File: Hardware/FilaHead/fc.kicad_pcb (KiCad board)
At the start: 2 copper layers, 55.9 x 48.3 mm, 7 parts, among them J0 Conn_2, J1 Conn_01x15_Female, J2 Conn_01x15_Female, J3 Conn_2

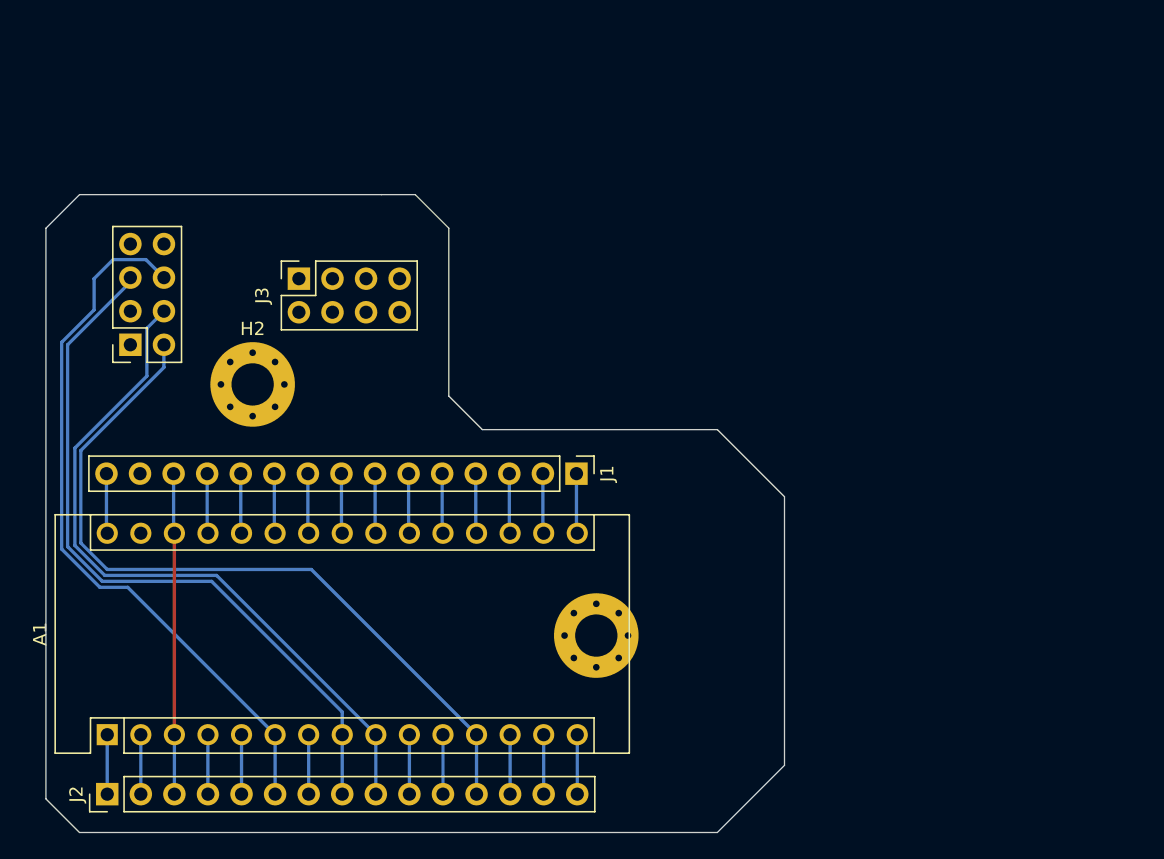
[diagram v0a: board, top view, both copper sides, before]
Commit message: Updated Fila Head
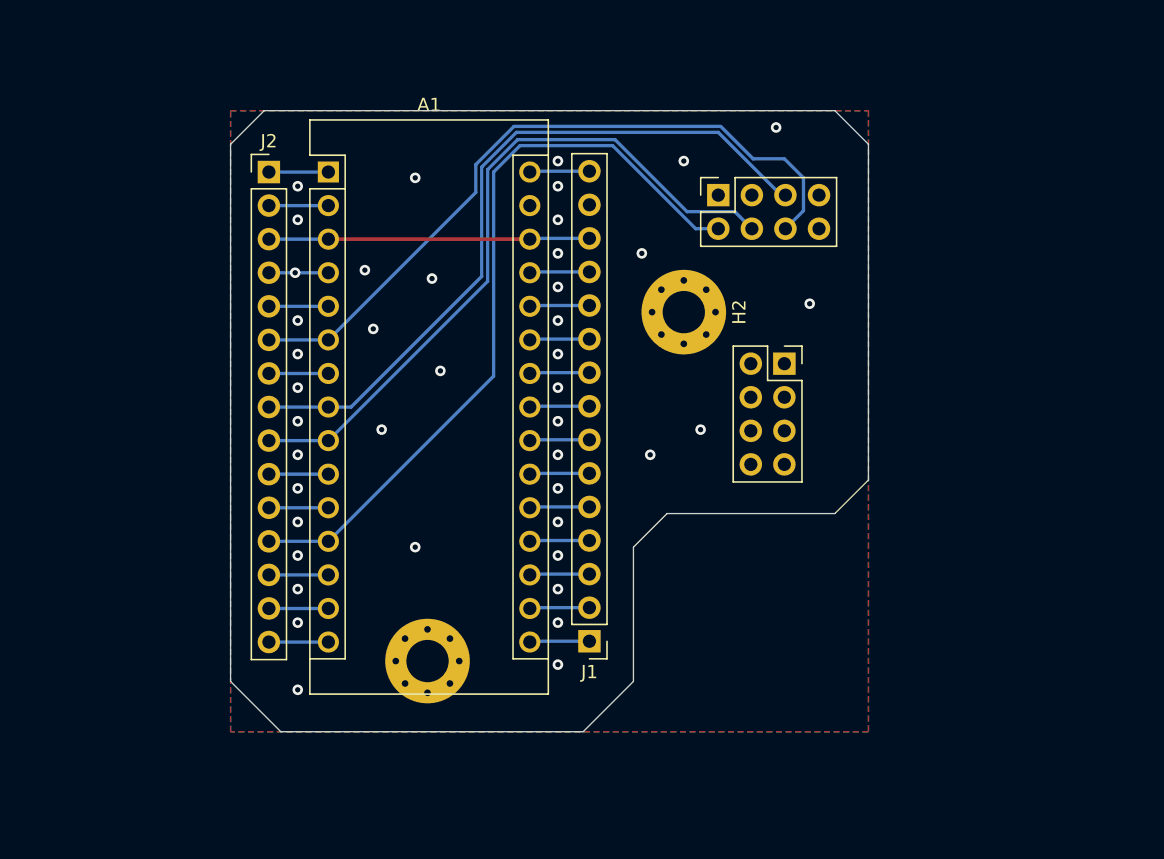
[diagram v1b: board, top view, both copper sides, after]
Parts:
- moved J2 48.6 mm to (103.2, 38.9), turned to 0 degrees
- moved J0 45.9 mm to (137.2, 40.7), turned to 90 degrees
- moved A1 45.7 mm to (107.7, 38.9), turned to 0 degrees
- moved J3 37.3 mm to (142.2, 53.4), turned to 0 degrees
- moved H2 33.1 mm to (134.6, 49.5), turned to 270 degrees
- moved H1 12.9 mm to (115.2, 75.9), turned to 270 degrees
- moved J1 12.7 mm to (127.5, 74.4), turned to 180 degrees
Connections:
- J0 pad 3: Net-(J0-Pad3) -> (no net)
- J0 pad 7: Net-(J0-Pad7) -> (no net)
- J3 pad 2: Net-(J3-Pad2) -> (no net)
- J3 pad 3: Net-(J3-Pad3) -> (no net)
- J3 pad 4: Net-(J3-Pad4) -> (no net)
- J3 pad 5: Net-(J3-Pad5) -> (no net)
- J3 pad 6: Net-(J3-Pad6) -> (no net)
- J3 pad 7: Net-(J3-Pad7) -> (no net)
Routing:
- net GND: vias 0 -> 43
- added copper zone on B.Cu, net GND
- added copper zone on F.Cu, net GND
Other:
- board size 55.9 x 48.3 mm -> 48.3 x 47 mm

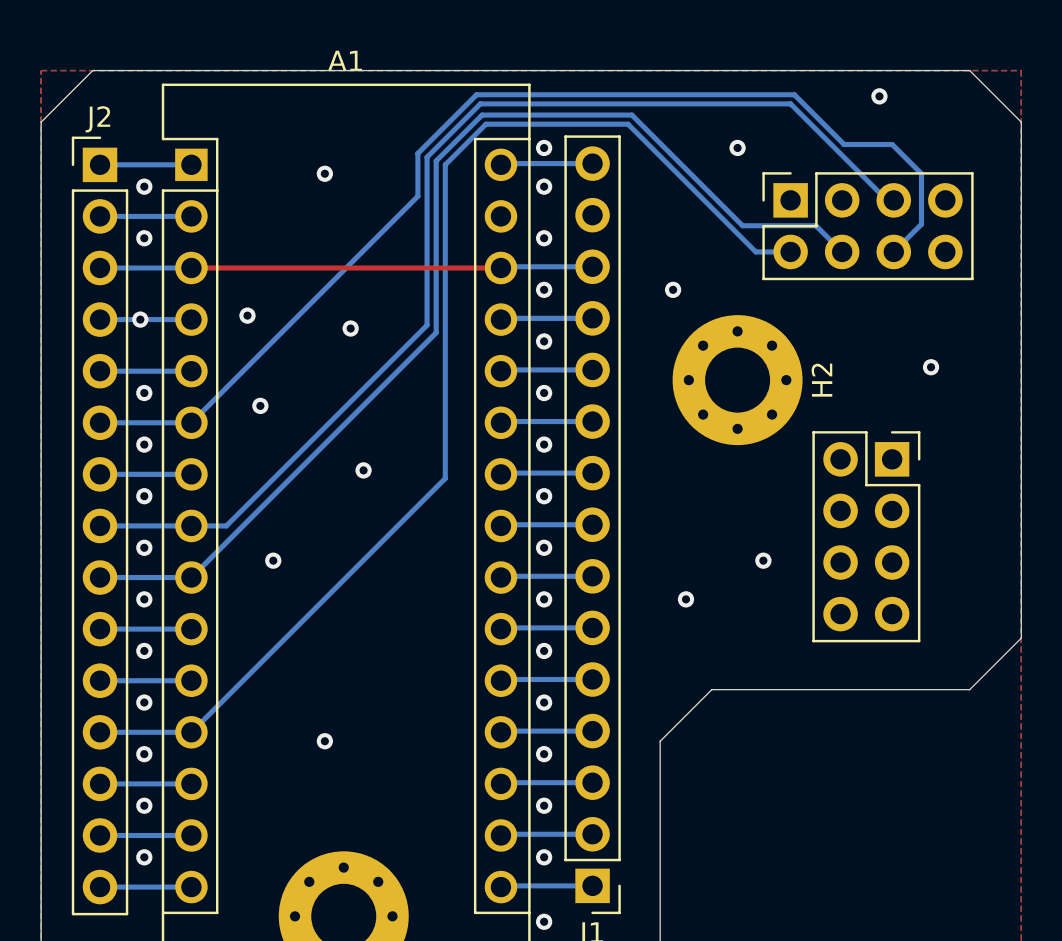
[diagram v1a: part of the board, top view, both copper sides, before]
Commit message: updated and generated Header connector
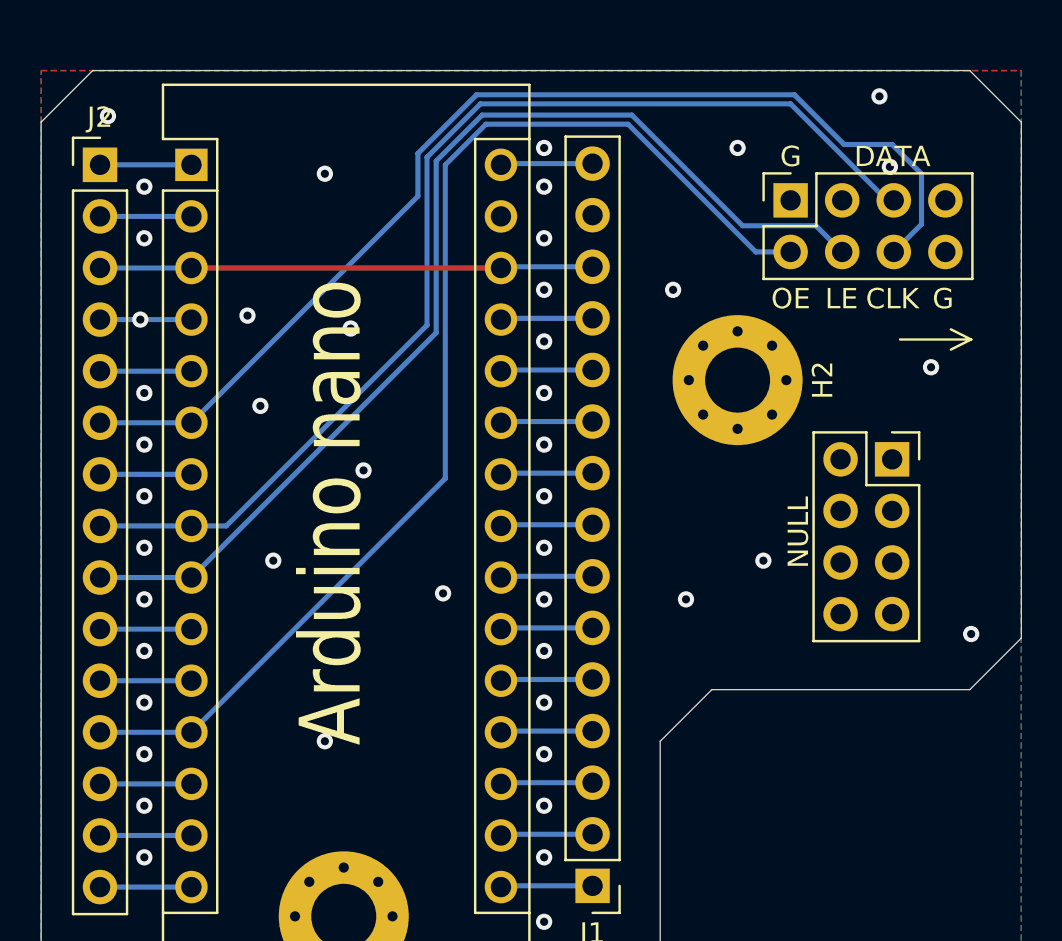
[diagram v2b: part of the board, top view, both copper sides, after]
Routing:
- net GND: vias 43 -> 47
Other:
- rule pad_to_mask_clearance: 0.051 -> 0
- board text added: "Arduino nano"
- board text added: "CLK"
- board text added: "DATA"
- board text added: "Filament Wall (2021.04) Header Connector v0.1 Sandbox Workshop Designed by Caorx Wangyw"
- board text added: "G"
- board text added: "JLCJLCJLCJLC"
- board text added: "LE"
- board text added: "NULL"
- board text added: "OE"

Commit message: updated packages
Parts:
- J0, J3: footprint Connector_PinSocket_2.54mm:PinSocket_2x04_P2.54mm_Vertical -> Connector_PinHeader_2.54mm:PinHeader_2x04_P2.54mm_Vertical
- moved J3 2.53 mm to (139.7, 53.3)
- moved J0 2.50 mm to (137.2, 43.2)
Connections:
- J0 pad 1: GND -> OE
- J0 pad 2: OE -> GND
- J0 pad 3: (no net) -> LE
- J0 pad 4: LE -> Net-(J0-Pad4)
- J0 pad 5: PWM5 -> CLK
- J0 pad 6: CLK -> PWM5
- J0 pad 7: (no net) -> GND
- J0 pad 8: GND -> Net-(J0-Pad8)
- J3 pad 1: GND -> Net-(J3-Pad1)
- J3 pad 2: (no net) -> GND
- J3 pad 3: (no net) -> Net-(J3-Pad3)
- J3 pad 4: (no net) -> Net-(J3-Pad4)
- J3 pad 5: (no net) -> Net-(J3-Pad5)
- J3 pad 6: (no net) -> Net-(J3-Pad6)
- J3 pad 7: (no net) -> GND
- J3 pad 8: GND -> Net-(J3-Pad8)
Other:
- board text added: "Filament Wall (2021.04) Header Connector v0.2 Sandbox Workshop Designed by Caorx Wangyw"
- board text removed: "Filament Wall (2021.04) Header Connector v0.1 Sandbox Workshop Designed by Caorx Wangyw"

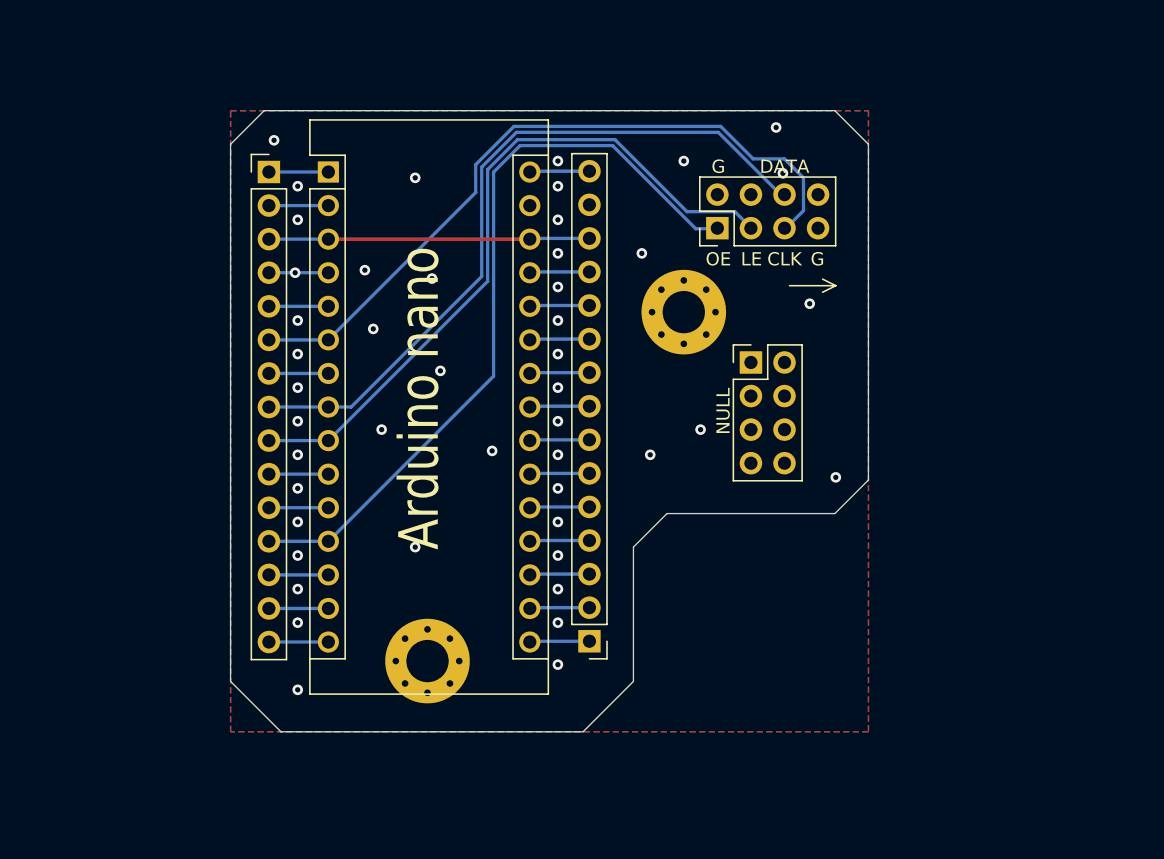
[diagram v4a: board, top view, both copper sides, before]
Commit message: updated FilaHead v0.3
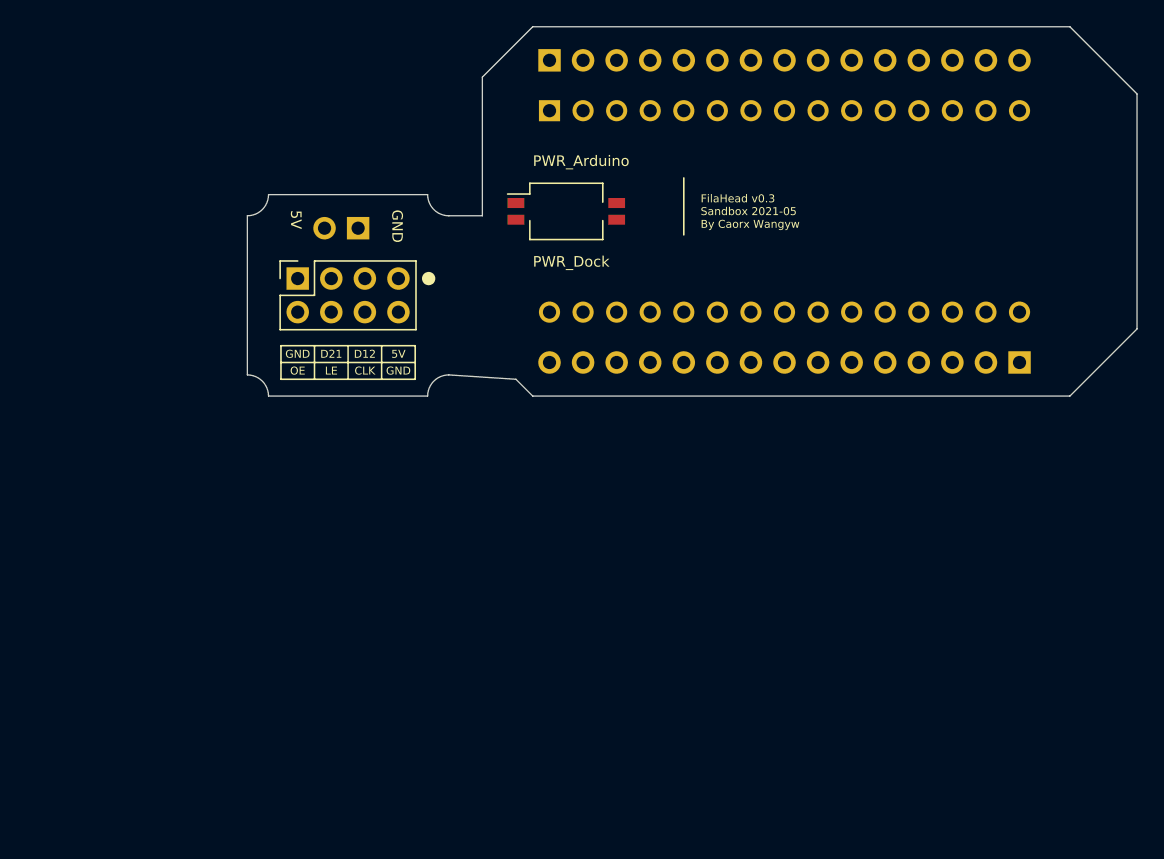
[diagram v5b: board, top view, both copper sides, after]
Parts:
- removed H1, H2: MountingHole_Pad, MountingHole:MountingHole_3.2mm_M3_Pad_Via
- removed J0: Conn_2, Connector_PinHeader_2.54mm:PinHeader_2x04_P2.54mm_Vertical
- added J4: Conn_01x15_Female, Connector_PinHeader_2.54mm:PinHeader_1x15_P2.54mm_Vertical, B.Cu at (124.5, 30.5)
- added SW1: PowerSel, Button_Switch_SMD:SW_DIP_SPSTx02_Slide_KingTek_DSHP02TS_W7.62mm_P1.27mm, F.Cu at (125.7, 41.9)
- A1, J1: moved to B.Cu
- J2: value Conn_01x15_Female -> Conn_2; footprint Connector_PinHeader_2.54mm:PinHeader_1x15_P2.54mm_Vertical -> Connector_PinSocket_2.54mm:PinSocket_2x04_P2.54mm_Vertical
- J3: value Conn_2 -> PWR_IN; footprint Connector_PinHeader_2.54mm:PinHeader_2x04_P2.54mm_Vertical -> Connector_PinHeader_2.54mm:PinHeader_1x02_P2.54mm_Horizontal; moved to B.Cu
- moved J1 38.8 mm to (160.0, 53.3), turned to 90 degrees
- moved J3 31.4 mm to (110.0, 43.2), turned to 90 degrees
- moved A1 17.4 mm to (124.5, 34.3), turned to 270 degrees
- moved J2 8.35 mm to (105.4, 47.0), turned to 90 degrees
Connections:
- J2 pad 1: TX1 -> GND
- J2 pad 2: RX0 -> OE
- J2 pad 3: A_RST -> Net-(J2-Pad3)
- J2 pad 4: GND -> LE
- J2 pad 5: D2 -> PWM5
- J2 pad 7: D4 -> /5v_CON2
- J2 pad 8: PWM5 -> GND
- J3 pad 1: Net-(J3-Pad1) -> GND
- J3 pad 2: GND -> /5v_PWR
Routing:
- net OE: track 58.1 -> 0.00 mm
- net PWM5: track 54.5 -> 0.00 mm
- net CLK: track 54.4 -> 0.00 mm
- net LE: track 53.7 -> 0.00 mm
- net A_RST: track 24.3 -> 0.00 mm
- net A_VIN: track 4.53 -> 0.00 mm
- net A_REF: track 4.53 -> 0.00 mm
- net A_3V3: track 4.53 -> 0.00 mm
- net A7: track 4.53 -> 0.00 mm
- net A6: track 4.53 -> 0.00 mm
- net A5: track 4.53 -> 0.00 mm
- net A4: track 4.53 -> 0.00 mm
- net A3: track 4.53 -> 0.00 mm
- net A2: track 4.53 -> 0.00 mm
- net A1: track 4.53 -> 0.00 mm
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- removed copper zone on B.Cu, net GND
- removed copper zone on F.Cu, net GND
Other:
- board size 48.3 x 47 mm -> 67.3 x 27.9 mm
- board text added: "5V"
- board text added: "D12"
- board text added: "D21"
- board text added: "FilaHead v0.3 Sandbox 2021-05 By Caorx Wangyw"
- board text added: "GND"
- board text added: "PWR_Arduino"
- board text added: "PWR_Dock"
- board text removed: "Arduino nano"
- board text removed: "DATA"
- board text removed: "Filament Wall (2021.04) Header Connector v0.2 Sandbox Workshop Designed by Caorx Wangyw"
- board text removed: "G"
- board text removed: "NULL"

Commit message: upload latest head PCB
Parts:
- moved SW1 3.81 mm to (129.5, 41.9)
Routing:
- net OE: track 0.00 -> 60.0 mm
- net LE: track 0.00 -> 48.5 mm
- net CLK: track 0.00 -> 40.9 mm
- net PWM5: track 0.00 -> 40.8 mm
- net /5v_PWR: track 0.00 -> 27.8 mm, vias 0 -> 2
- net A_RST: track 0.00 -> 22.9 mm
- net /5v_CON2: track 0.00 -> 16.6 mm
- net A_5V: track 0.00 -> 14.8 mm
- net D13: track 0.00 -> 3.81 mm
- net A_VIN: track 0.00 -> 3.81 mm
- net A_REF: track 0.00 -> 3.81 mm
- net A_3V3: track 0.00 -> 3.81 mm
- net A7: track 0.00 -> 3.81 mm
- net A6: track 0.00 -> 3.81 mm
- net A5: track 0.00 -> 3.81 mm
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- added copper zone on B.Cu, net GND
- added copper zone on F.Cu, net GND
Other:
- outline, holes or cut-outs redrawn

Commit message: optimized pcb
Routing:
- net GND: track 0.00 -> 6.50 mm, vias 83 -> 85
- net PWM5: track 40.8 -> 41.6 mm
- net CLK: track 40.9 -> 41.6 mm
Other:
- outline, holes or cut-outs redrawn

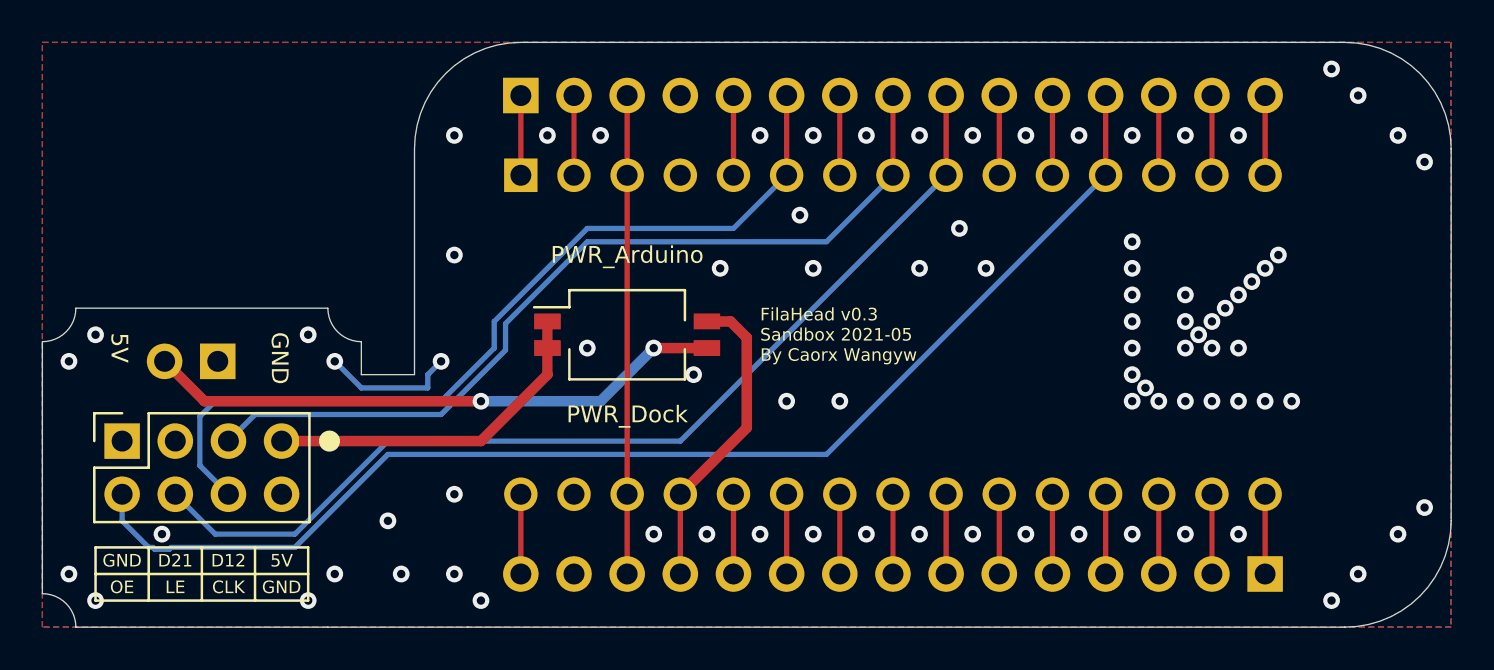
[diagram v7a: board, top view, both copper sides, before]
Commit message: rounded corners
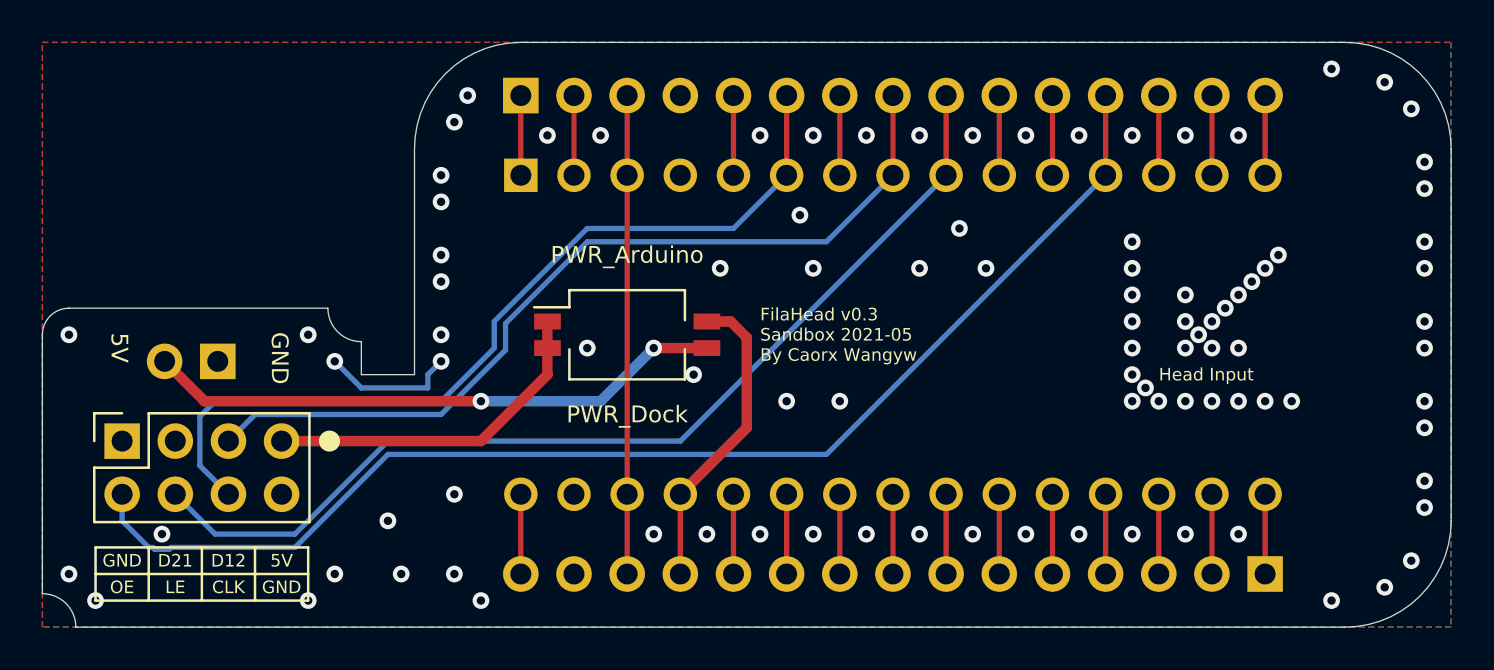
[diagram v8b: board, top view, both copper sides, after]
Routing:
- net GND: vias 85 -> 97
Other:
- outline, holes or cut-outs redrawn
- board text added: "<- USB | Arduino"
- board text added: "Head Input"
